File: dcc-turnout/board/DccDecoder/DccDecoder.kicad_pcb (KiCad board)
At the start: 4 copper layers, 95 x 46 mm, 63 parts, among them J1 Conn_01x02, J2 Conn_01x02, J3 Conn_01x03, J4 Conn_01x02, J5 Conn_01x02, J6 Conn_01x02, J7 Conn_01x04, Q1 BC857, Q2 BC817, Q3 2N7002, Q4 BSS308, U1 AMS1117-3.3, U2 6N137S1, U3 PC817, U4 TPS54331D

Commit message: Changes after test
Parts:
- added H4: MountingHole_Pad, MountingHole:MountingHole_2.7mm_M2.5_DIN965_Pad, F.Cu at (24.0, 24.0)
- added J8: Conn_01x02, TerminalBlock_Phoenix:TerminalBlock_Phoenix_PT-1,5-2-3.5-H_1x02_P3.50mm_Horizontal, F.Cu at (36.8, 25.4)
- added JP8: SolderJumper_2_Open, Jumper:SolderJumper-2_P1.3mm_Open_RoundedPad1.0x1.5mm, F.Cu at (77.2, 45.5)
- D1: footprint Diode_SMD:D_SOD-323 -> Diode_SMD:D_SOD-323_HandSoldering
- D7: footprint Diode_SMD:D_SOD-123 -> Diode_SMD:D_SMA
- J4, J5, J6: footprint Connector_PinHeader_2.54mm:PinHeader_1x02_P2.54mm_Vertical -> TerminalBlock_Phoenix:TerminalBlock_Phoenix_PT-1,5-2-3.5-H_1x02_P3.50mm_Horizontal
- J7: footprint Connector_JST:JST_XH_B4B-XH-A_1x04_P2.50mm_Vertical -> Connector_JST:JST_XH_S4B-XH-A_1x04_P2.50mm_Horizontal
- moved D3 13.3 mm to (27.9, 42.4)
- moved JP7 7.76 mm to (63.5, 57.2), turned to 90 degrees
- moved J2 6.75 mm to (28.9, 31.8)
- moved JP5 5.99 mm to (85.7, 57.2), turned to 90 degrees
- moved JP6 5.83 mm to (34.3, 57.2), turned to 90 degrees
- moved J1 5.33 mm to (26.7, 52.3)
- moved J3 5.25 mm to (23.4, 41.4)
- moved R7 4.83 mm to (37.3, 32.4)
- moved D8 4.62 mm to (32.8, 33.4), turned to 90 degrees
- moved R9 4.62 mm to (61.0, 61.6), turned to 90 degrees
- moved D5 4.40 mm to (63.5, 61.6), turned to 90 degrees
- moved D6 3.23 mm to (85.7, 61.6), turned to 90 degrees
- moved D4 3.13 mm to (34.3, 61.5), turned to 90 degrees
- moved R6 2.95 mm to (31.8, 61.4), turned to 90 degrees
- moved J5 2.79 mm to (67.3, 61.0), turned to 0 degrees
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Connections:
- C3 pad 1: +5V -> /5V_iFace
- J7 pad 1: +5V -> /5V_iFace
- R4 pad 2: +5V -> /5V_iFace
- R5 pad 2: +5V -> /5V_iFace
- U2 pad 8: +5V -> /5V_iFace
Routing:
- net /5V_iFace: track 0.00 -> 36.2 mm
- net +5V: track 56.7 -> 27.6 mm
- net +3V3: track 20.8 -> 27.9 mm
- net Net-(Q2-Pad1): track 8.17 -> 2.78 mm
- net /Dcc Interface/J: track 51.5 -> 56.6 mm
- net Vdrive: track 41.1 -> 36.3 mm, vias 6 -> 5
- net /Power Distribution/Vin: track 22.8 -> 27.4 mm
- net /Dcc Interface/K: track 68.4 -> 71.9 mm
- net Net-(D8-Pad1): track 2.06 -> 4.95 mm
- net GND: vias 10 -> 9
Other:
- board text added: "+ 12V DC -"
- board text added: "-"
- board text added: "- 3.3v +"
- board text added: "- 5v +"
- board text added: "- VDrive +"
- board text added: "12V DC"
- board text added: "DCC Signal"
- board text added: "Dcc Power Distribution Board v0.3.0"
- board text added: "GND DCC ACK +5V"
- board text added: "JP1 & JP2 cut to remove DCC Power and ACK JP3 & JP4 cut to remove DCC Power JP5, JP6 & JP7 cut to disable led (3V, 5V, VDrive) JP8 solder to power Iface from 5V"
- board text removed: "3.3vLed"
- board text removed: "5vLed"
- board text removed: "Dcc Power Distribution Board"
- board text removed: "Dcc Power Distribution Board v0.2.0"
- board text removed: "V 0.0.1 Power Switch Prototype"
- board text removed: "VDriveLed"

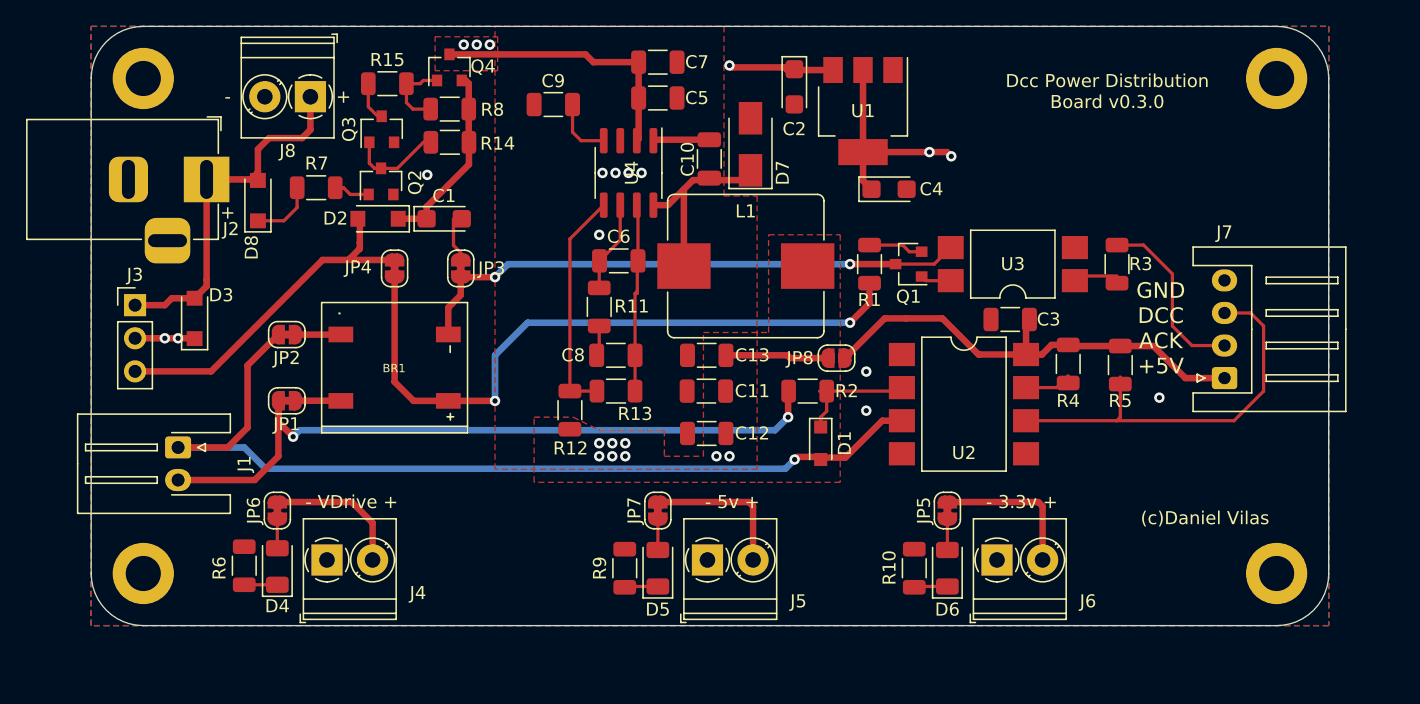
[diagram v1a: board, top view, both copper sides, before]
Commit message: Dcc Decoder update without power dist
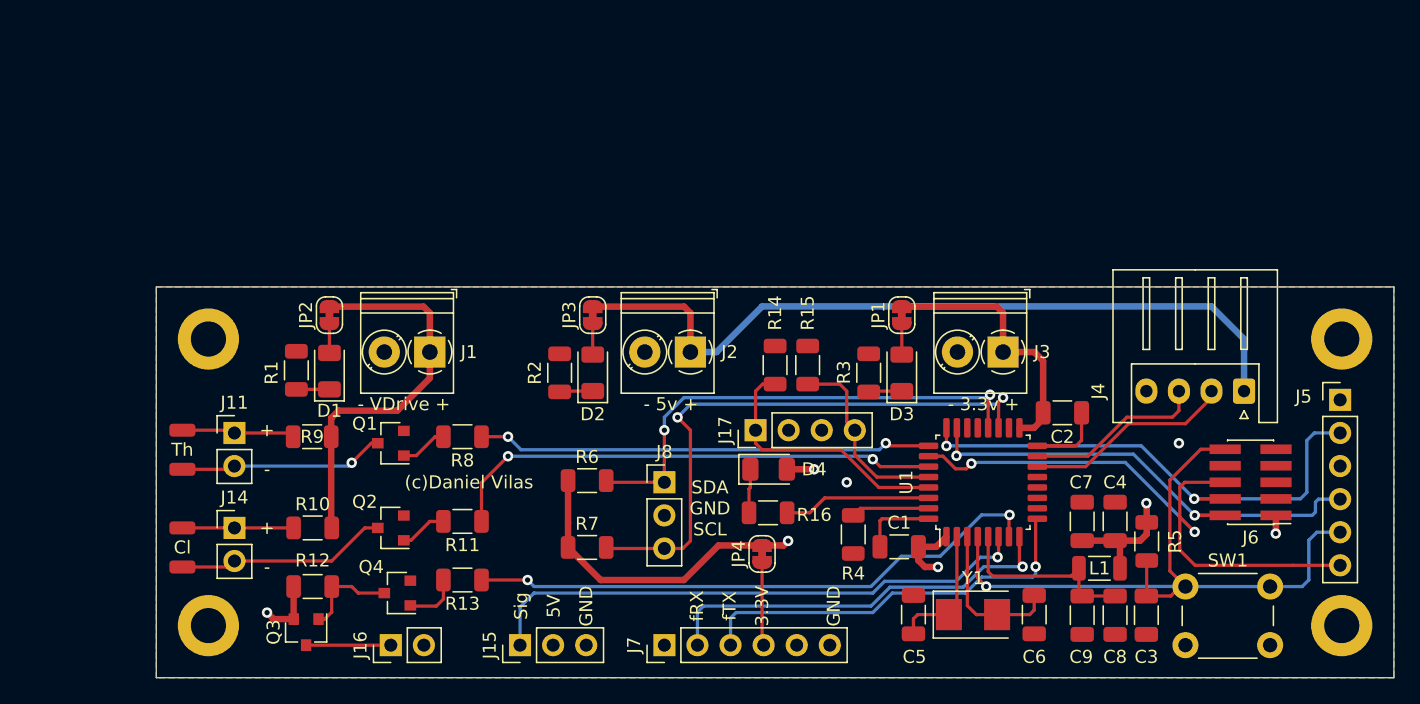
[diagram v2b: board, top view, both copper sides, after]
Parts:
- removed BR1: DB107S, Project:DIOB_DB107S
- removed C10: 100nf 1m, Capacitor_SMD:C_1206_3216Metric
- removed C11, C12, C13: 10uf 2m, Capacitor_SMD:C_1206_3216Metric
- removed the D1 at (76.0, 52.0)
- removed the D2 at (42.0, 34.8)
- removed the D3 at (27.9, 42.4)
- removed D7: SS24A+, Diode_SMD:D_SMA
- removed D8: GS1510FL, Project:D_SOD-123FL
- removed the J2 at (28.9, 31.8)
- removed the J3 at (23.4, 41.4)
- removed the J4 at (38.1, 61.0)
- removed the JP1 at (35.0, 48.7)
- removed the JP2 at (35.0, 43.7)
- removed the JP3 at (48.4, 38.6)
- removed JP8: SolderJumper_2_Open, Jumper:SolderJumper-2_P1.3mm_Open_RoundedPad1.0x1.5mm
- removed the R1 at (79.8, 38.2)
- removed the R2 at (75.0, 48.0)
- removed the R3 at (98.8, 38.2)
- removed U2: 6N137S1, Package_DIP:SMDIP-8_W9.53mm
- removed U3: PC817, Package_DIP:SMDIP-4_W9.53mm
- removed U4: TPS54331D, Package_SO:SOIC-8_3.9x4.9mm_P1.27mm
- added D4: LED, LED_SMD:LED_1206_3216Metric, F.Cu at (72.0, 54.0)
- added J10: Conn_01x01, Connector_Wire:SolderWirePad_1x01_SMD_1x2mm, F.Cu at (27.0, 54.0)
- added J11: Conn_01x02, Connector_PinHeader_2.54mm:PinHeader_1x02_P2.54mm_Vertical, F.Cu at (31.0, 51.2)
- added J12: Conn_01x01, Connector_Wire:SolderWirePad_1x01_SMD_1x2mm, F.Cu at (27.0, 58.5)
- added J13: Conn_01x01, Connector_Wire:SolderWirePad_1x01_SMD_1x2mm, F.Cu at (27.0, 61.5)
- added J14: Conn_01x02, Connector_PinHeader_2.54mm:PinHeader_1x02_P2.54mm_Vertical, F.Cu at (31.0, 58.5)
- added J15: Conn_01x03, Connector_PinHeader_2.54mm:PinHeader_1x03_P2.54mm_Vertical, F.Cu at (52.9, 67.5)
- added J16: Conn_01x02, Connector_PinHeader_2.54mm:PinHeader_1x02_P2.54mm_Vertical, F.Cu at (43.0, 67.5)
- added J17: Conn_01x04, Connector_PinHeader_2.54mm:PinHeader_1x04_P2.54mm_Vertical, F.Cu at (71.0, 51.0)
- added J5: Conn_01x06, Connector_PinHeader_2.54mm:PinHeader_1x06_P2.54mm_Vertical, F.Cu at (115.9, 48.7)
- added J6: Conn_02x05 Odd_Even, Connector_PinHeader_1.27mm:PinHeader_2x05_P1.27mm_Vertical_SMD, F.Cu at (109.0, 55.0)
- added J7: Conn_01x06, Connector_PinHeader_2.54mm:PinHeader_1x06_P2.54mm_Vertical, F.Cu at (64.0, 67.5)
- added J9: Conn_01x01, Connector_Wire:SolderWirePad_1x01_SMD_1x2mm, F.Cu at (27.0, 51.0)
- added R10: 1K, Resistor_SMD:R_1206_3216Metric, F.Cu at (37.0, 58.5)
- added R16: 100, Resistor_SMD:R_1206_3216Metric, F.Cu at (72.0, 57.3)
- added R6: 1K, Resistor_SMD:R_1206_3216Metric, F.Cu at (58.1, 54.9)
- added R9: 1K, Resistor_SMD:R_1206_3216Metric, F.Cu at (37.0, 51.5)
- added SW1: SW_Push, Button_Switch_THT:SW_PUSH_6mm, F.Cu at (104.0, 63.0)
- added Y1: 8MHz, Crystal:Crystal_SMD_5032-2Pin_5.0x3.2mm, F.Cu at (87.7, 65.2)
- C1, C2: value 10uf -> 100nf; footprint Capacitor_Tantalum_SMD:CP_EIA-3216-18_Kemet-A -> Capacitor_SMD:C_1206_3216Metric
- C3: value 10uf -> 100nf
- C4: value 10uf -> 1uF; footprint Capacitor_Tantalum_SMD:CP_EIA-3216-18_Kemet-A -> Capacitor_SMD:C_1206_3216Metric
- C5: value 10uf 2m -> 20pf
- C6: value 10pf -> 20pf
- C7: value 10uf 2m -> 10nF
- C8: value 5.6nf -> 1uF
- C9: value 8.2nf -> 10nF
- J1: footprint Connector_JST:JST_XH_S2B-XH-A-1_1x02_P2.50mm_Horizontal -> TerminalBlock_Phoenix:TerminalBlock_Phoenix_PT-1,5-2-3.5-H_1x02_P3.50mm_Horizontal
- J8: value Conn_01x02 -> Conn_01x03; footprint TerminalBlock_Phoenix:TerminalBlock_Phoenix_PT-1,5-2-3.5-H_1x02_P3.50mm_Horizontal -> Connector_PinHeader_2.54mm:PinHeader_1x03_P2.54mm_Vertical
- JP4: value Jumper_NC -> Jumper_2_Bridged
- L1: value 22uH 75mO -> 10uH; footprint Project:L_Bourns_SRP1035 -> Inductor_SMD:L_1206_3216Metric
- Q1: value BC857 -> NXV55UNR
- Q2: value BC817 -> NXV55UNR
- Q3: value 2N7002 -> NXV90EPR
- Q4: value BSS308 -> NXV55UNR
- R11: value 5.62K -> 1K
- R12: value 10.2K -> 1K
- R13: value 1.96K -> 1K
- R14, R15, R7, R8: value 100K -> 1K
- U1: value AMS1117-3.3 -> STM32F030K6Tx; footprint Package_TO_SOT_SMD:SOT-223-3_TabPin2 -> Package_QFP:LQFP-32_7x7mm_P0.8mm
- moved H4 101.1 mm to (116.0, 66.0)
- moved H2 82.1 mm to (29.0, 66.0)
- moved C9 56.4 mm to (96.1, 65.2), turned to 270 degrees
- moved C7 48.0 mm to (96.1, 58.0), turned to 90 degrees
- moved C5 44.2 mm to (83.1, 65.2), turned to 90 degrees
- moved C8 43.2 mm to (98.6, 65.2), turned to 270 degrees
- moved C1 43.1 mm to (82.0, 59.9)
- moved Q1 42.1 mm to (43.0, 52.0)
- moved C6 41.9 mm to (92.4, 65.2), turned to 270 degrees
- moved Q4 40.5 mm to (43.5, 63.5), turned to 180 degrees
- moved J8 40.2 mm to (64.0, 55.0), turned to 0 degrees
- moved Q3 39.0 mm to (36.5, 66.5), turned to 270 degrees
- moved R15 38.8 mm to (75.0, 46.0), turned to 270 degrees
- moved JP4 35.7 mm to (71.5, 60.5)
- moved L1 35.7 mm to (97.4, 61.6)
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- renumbered D4 to D1, D5 to D2, D6 to D3, J5 to J2, J6 to J3, J7 to J4, JP5 to JP1, JP6 to JP2, JP7 to JP3, R6 to R1, R9 to R2, R10 to R3
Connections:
- C1 pad 1: /Power Distribution/_DccVinP -> GND
- C1 pad 2: GND -> +3V3
- C2 pad 1: +5V -> GND
- C2 pad 2: GND -> +3V3
- C3 pad 1: /5V_iFace -> /uC 030K6/NRST
- C5 pad 1: Vdrive -> /uC 030K6/PF0
- C6 pad 1: Net-(C6-Pad1) -> /uC 030K6/PF1
- C7 pad 1: Vdrive -> +3V3
- C8 pad 1: Net-(C8-Pad1) -> /uC 030K6/_VDDA
- C9 pad 1: Net-(C9-Pad1) -> /uC 030K6/_VDDA
- J1 pad 1: /Dcc Interface/K -> Vdrive
- J1 pad 2: /Dcc Interface/J -> GND
- J2 pad 1: GND -> +5V
- J2 pad 2: +5V -> GND
- J3 pad 1: GND -> +3V3
- J3 pad 2: +3V3 -> GND
- J4 pad 1: /5V_iFace -> +5V
- J8 pad 1: /Power Distribution/Vin -> /SDA
- JP4 pad 1: /Dcc Interface/DccP+ -> /F_Vcc
- JP4 pad 2: /Dcc Interface/DccPower -> +3V3
- L1 pad 1: /Power Distribution/_PH -> /uC 030K6/_VDDA
- L1 pad 2: +5V -> +3V3
- Q1 pad 2: Net-(Q1-Pad2) -> GND
- Q1 pad 3: /Dcc Interface/DccP- -> Net-(J10-Pad1)
- Q2 pad 3: Net-(Q2-Pad3) -> Net-(J13-Pad1)
- Q3 pad 1: Net-(Q2-Pad3) -> Net-(Q3-Pad1)
- Q3 pad 2: GND -> +5V
- Q3 pad 3: Net-(Q3-Pad3) -> Net-(J16-Pad1)
- Q4 pad 2: /Power Distribution/_DccVinP -> GND
- Q4 pad 3: Vdrive -> Net-(Q3-Pad1)
- R11 pad 1: Net-(C6-Pad1) -> /ClosedLed
- R11 pad 2: Net-(C8-Pad1) -> Net-(Q2-Pad1)
- R12 pad 1: +5V -> Net-(Q3-Pad1)
- R12 pad 2: Net-(R12-Pad2) -> +5V
- R13 pad 1: Net-(R12-Pad2) -> /ReleEn
- R13 pad 2: GND -> Net-(Q4-Pad1)
- R14 pad 1: /Power Distribution/_DccVinP -> GND
- R14 pad 2: Net-(Q2-Pad3) -> /CfgBasic
- R15 pad 1: Net-(Q3-Pad3) -> GND
- R15 pad 2: Net-(Q4-Pad1) -> /CfgAdvanced
- R4 pad 1: Net-(R4-Pad1) -> /uC 030K6/BOOT0
- R4 pad 2: /5V_iFace -> GND
- R5 pad 1: /_dcc -> +3V3
- R5 pad 2: /5V_iFace -> /uC 030K6/NRST
- R7 pad 1: Net-(Q2-Pad1) -> +3V3
- R7 pad 2: Net-(D8-Pad1) -> /SCL
- R8 pad 1: /Power Distribution/_DccVinP -> /ThrownLed
- R8 pad 2: Net-(Q4-Pad1) -> Net-(Q1-Pad1)
- U1 pad 1: GND -> +3V3
- U1 pad 2: +3V3 -> /uC 030K6/PF0
- U1 pad 3: +5V -> /uC 030K6/PF1
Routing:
- net /Dcc Interface/K: track 71.9 -> 0.00 mm, vias 1 -> 0
- net /Dcc Interface/J: track 56.6 -> 0.00 mm, vias 2 -> 0
- net /uC 030K6/NRST: track 0.00 -> 54.7 mm, vias 0 -> 1
- net /Dcc Interface/DccP+: track 51.8 -> 0.00 mm, vias 2 -> 0
- net /uC 030K6/PB3: track 0.00 -> 46.1 mm, vias 0 -> 2
- net /SCL: track 0.00 -> 44.7 mm, vias 0 -> 2
- net /ReleEn: track 0.00 -> 44.7 mm, vias 0 -> 2
- net /Dcc Interface/DccP-: track 43.4 -> 0.00 mm, vias 2 -> 0
- net /ServoSig: track 0.00 -> 42.8 mm, vias 0 -> 1
- net /uC 030K6/PA14: track 0.00 -> 40.1 mm, vias 0 -> 2
- net /ClosedLed: track 0.00 -> 38.5 mm, vias 0 -> 2
- net /SDA: track 0.00 -> 37.8 mm, vias 0 -> 2
- net /uC 030K6/PA13: track 0.00 -> 36.9 mm, vias 0 -> 2
- net +5V: track 27.6 -> 64.4 mm, vias 9 -> 1
- net /5V_iFace: track 36.2 -> 0.00 mm
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- removed copper zone on F.Cu, net +5V
- removed copper zone on F.Cu, net Vdrive
- removed copper zone on In2.Cu, net Vdrive
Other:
- board size 95 x 46 mm -> 95 x 30 mm
- board text added: "3.3V"
- board text added: "5V"
- board text added: "Advanced"
- board text added: "Basic"
- board text added: "Cl"
- board text added: "Closed"
- board text added: "Config"
- board text added: "DO"
- board text added: "GND"
- board text added: "Gnd"
- board text added: "Rst"
- board text added: "Run"
- board text added: "SCL"
- board text added: "SDA"
- board text added: "SDA GND SCL"
- board text added: "SWCLK"
- board text added: "SWDIO"
- board text added: "Sig"
- board text added: "Th"
- board text added: "Thrown"
- board text added: "Vcc"
- board text added: "fRX"
- board text added: "fTX"
- board text removed: "+ 12V DC -"
- board text removed: "12V DC"
- board text removed: "DCC Signal"
- board text removed: "Dcc Power Distribution Board v0.3.0"
- board text removed: "JP1 & JP2 cut to remove DCC Power and ACK JP3 & JP4 cut to remove DCC Power JP5, JP6 & JP7 cut to disable led (3V, 5V, VDrive) JP8 solder to power Iface from 5V"
- board text removed: "Vin VDrive Dcc"

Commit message: Choosed It2
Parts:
- added JP5: Jumper_2_Open, Jumper:SolderJumper-2_P1.3mm_Open_RoundedPad1.0x1.5mm, F.Cu at (61.0, 62.0)
- added Q5: NXV90EPR, Package_TO_SOT_SMD:SOT-23, F.Cu at (64.5, 65.0)
- added Q6: NXV55UNR, Package_TO_SOT_SMD:SOT-23, F.Cu at (73.5, 65.5)
- added R17: 1K, Resistor_SMD:R_1206_3216Metric, F.Cu at (69.0, 65.5)
- added R18: 1K, Resistor_SMD:R_1206_3216Metric, F.Cu at (78.0, 65.5)
- moved J5 58.2 mm to (58.5, 58.5), turned to 90 degrees
- moved J7 53.8 mm to (117.5, 61.5), turned to 180 degrees
- moved R6 51.0 mm to (109.0, 52.0)
- moved R7 46.6 mm to (104.0, 52.0), turned to 180 degrees
- moved J8 46.1 mm to (110.0, 58.5), turned to 270 degrees
- moved JP4 42.5 mm to (114.0, 61.5), turned to 270 degrees
- moved J6 23.0 mm to (88.5, 44.5), turned to 270 degrees
- moved R1 22.4 mm to (57.0, 53.5), turned to 270 degrees
- moved D1 18.7 mm to (57.0, 47.5)
- moved JP2 18.7 mm to (57.0, 43.0)
- moved D3 17.2 mm to (65.0, 47.5)
- moved JP1 17.2 mm to (65.0, 43.0)
- moved J3 17.0 mm to (73.0, 45.0)
- moved R3 16.2 mm to (65.0, 53.5), turned to 270 degrees
- moved J2 14.5 mm to (51.5, 45.0)
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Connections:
- J15 pad 2: +5V -> /Out Puts/_ServoPwr
- U1 pad 10: (no net) -> /ServoEn
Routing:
- net /ServoEn: track 0.00 -> 19.7 mm, vias 0 -> 2
- net /uC 030K6/NRST: track 54.7 -> 72.3 mm, vias 1 -> 3
- net /Out Puts/_ServoPwr: track 0.00 -> 15.2 mm
- net /SCL: track 44.7 -> 29.6 mm, vias 2 -> 1
- net +5V: track 64.4 -> 78.8 mm, vias 1 -> 3
- net /uC 030K6/PB3: track 46.1 -> 32.5 mm, vias 2 -> 3
- net Net-(Q5-Pad1): track 0.00 -> 8.30 mm
- net +3V3: track 63.8 -> 71.8 mm, vias 5 -> 6
- net Vdrive: track 30.2 -> 38.0 mm, vias 0 -> 2
- net /ClosedLed: track 38.5 -> 46.2 mm
- net /CfgBasic: track 20.4 -> 13.1 mm, vias 0 -> 1
- net /CfgAdvanced: track 14.8 -> 20.4 mm, vias 0 -> 1
- net /ThrownLed: track 35.0 -> 40.1 mm
- net /F_TX: track 31.3 -> 27.1 mm
- net /F_RX: track 31.4 -> 27.2 mm
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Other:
- outline, holes or cut-outs redrawn
- board text added: "DCC Turnout Board V0.4.0"
- board text added: "DIO"
- board text added: "SCL GND SDA"
- board text removed: "SDA GND SCL"

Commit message: Fab iteration
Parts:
- Y1: footprint Crystal:Crystal_SMD_5032-2Pin_5.0x3.2mm -> Project:HC-49SM8MH
- moved C5 8.13 mm to (75.0, 66.0)
- moved R18 4.00 mm to (78.0, 61.5), turned to 180 degrees
- moved Q6 3.81 mm to (72.0, 62.0), turned to 270 degrees
- moved Y1 3.21 mm to (84.5, 66.0)
- moved C6 1.16 mm to (93.5, 66.0)
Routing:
- net /uC 030K6/PF0: track 10.8 -> 18.5 mm
- net /ServoEn: track 19.7 -> 17.1 mm
- net Net-(Q5-Pad1): track 8.30 -> 10.6 mm
- net /uC 030K6/PF1: track 11.6 -> 13.1 mm

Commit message: Update to Production
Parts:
- removed J5: Conn_01x06, Connector_PinHeader_2.54mm:PinHeader_1x06_P2.54mm_Vertical
- J6: footprint Connector_PinHeader_1.27mm:PinHeader_2x05_P1.27mm_Vertical_SMD -> Connector_PinHeader_1.27mm:PinHeader_2x05_P1.27mm_Vertical
- moved J6 2.55 mm to (91.0, 44.0)
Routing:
- net /uC 030K6/PA14: track 43.3 -> 8.52 mm, vias 1 -> 0
- net /uC 030K6/PA13: track 40.7 -> 9.22 mm, vias 1 -> 0
- net +3V3: track 71.8 -> 44.2 mm, vias 6 -> 5
- net /uC 030K6/NRST: track 72.3 -> 47.1 mm, vias 3 -> 2
- net /uC 030K6/PB3: track 32.5 -> 14.1 mm, vias 3 -> 2
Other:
- net class Power: clearance 0.3 -> 0.25
- board text removed: "DIO"
- board text removed: "DO"
- board text removed: "Gnd"
- board text removed: "Rst"
- board text removed: "SWCLK"
- board text removed: "SWDIO"
- board text removed: "Vcc"
